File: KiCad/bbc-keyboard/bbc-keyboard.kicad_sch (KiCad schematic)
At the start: 29 parts

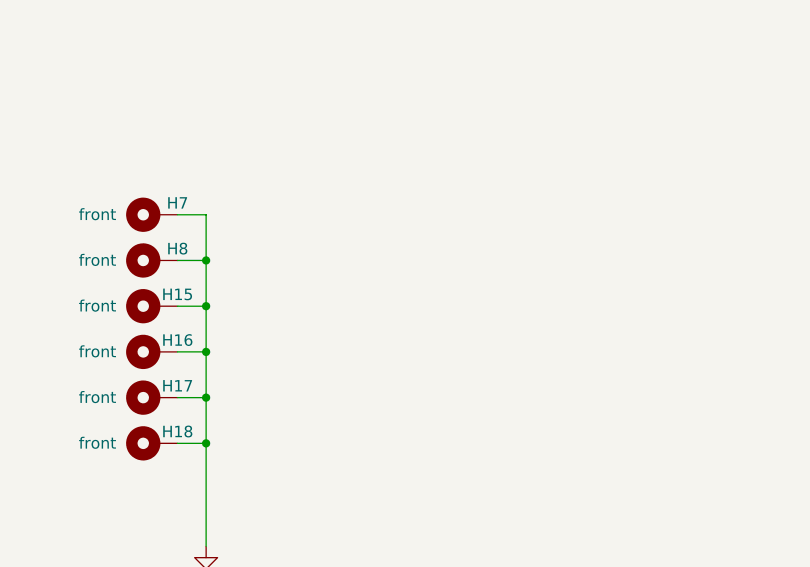
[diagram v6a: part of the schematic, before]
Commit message: mounting holes, symbols for stabilizers
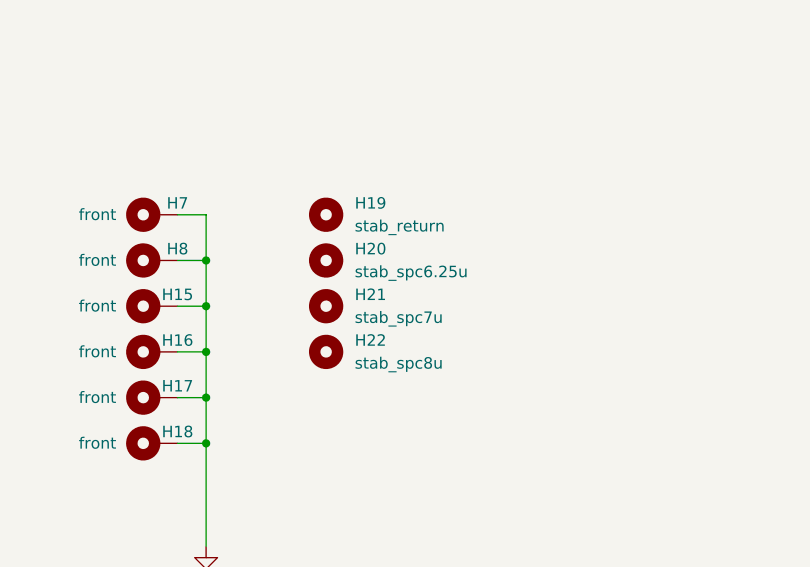
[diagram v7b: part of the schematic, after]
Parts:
- added H19: stab_return, Mounting_Keyboard_Stabilizer:Stabilizer_Cherry_MX_2.00u, symbol Mechanical:MountingHole
- added H20: stab_spc6.25u, Mounting_Keyboard_Stabilizer:Stabilizer_Cherry_MX_6.25u, symbol Mechanical:MountingHole
- added H21: stab_spc7u, Mounting_Keyboard_Stabilizer:Stabilizer_Cherry_MX_7.00u, symbol Mechanical:MountingHole
- added H22: stab_spc8u, Mounting_Keyboard_Stabilizer:Stabilizer_Cherry_MX_8.00u, symbol Mechanical:MountingHole
- H10, H11, H12, H13, H14, H9: footprint MountingHole:MountingHole_6.5mm -> Holes:SquareHole_6.5mm
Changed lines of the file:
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@@
       (effects (font (size 1.27 1.27)) (justify left))
     )
-    (property "Footprint" "MountingHole:MountingHole_6.5mm" (id 2) (at 57.15 160.655 0)
+    (property "Footprint" "Holes:SquareHole_6.5mm" (id 2) (at 57.15 160.655 0)
       (effects (font (size 1.27 1.27)) hide)
     )
@@
       (effects (font (size 1.27 1.27)) (justify left))
     )
-    (property "Footprint" "MountingHole:MountingHole_6.5mm" (id 2) (at 57.15 155.575 0)
+    (property "Footprint" "Holes:SquareHole_6.5mm" (id 2) (at 57.15 155.575 0)
       (effects (font (size 1.27 1.27)) hide)
     )
@@
       (effects (font (size 1.27 1.27)) (justify left))
     )
-    (property "Footprint" "MountingHole:MountingHole_6.5mm" (id 2) (at 57.15 150.495 0)
+    (property "Footprint" "Holes:SquareHole_6.5mm" (id 2) (at 57.15 150.495 0)
       (effects (font (size 1.27 1.27)) hide)
     )
@@
       (effects (font (size 1.27 1.27)) (justify left))
     )
-    (property "Footprint" "MountingHole:MountingHole_6.5mm" (id 2) (at 57.15 165.735 0)
+    (property "Footprint" "Holes:SquareHole_6.5mm" (id 2) (at 57.15 165.735 0)
       (effects (font (size 1.27 1.27)) hide)
     )
@@
     (pin "1")
   )
+  (symbol (lib_id "Mechanical:MountingHole") (at 109.855 150.495 0) (unit 1)
+    (in_bom yes) (on_board yes) (fields_autoplaced)
+    (property "Reference" "H21" (id 0) (at 113.03 149.2249 0)
+      (effects (font (size 1.27 1.27)) (justify left))
+    )
+    (property "Value" "stab_spc7u" (id 1) (at 113.03 151.7649 0)
+      (effects (font (size 1.27 1.27)) (justify left))
+    )
+    (property "Footprint" "Mounting_Keyboard_Stabilizer:Stabilizer_Cherry_MX_7.00u" (id 2) (at 109.855 150.495 0)
+      (effects (font (size 1.27 1.27)) hide)
+    )
+    (property "Datasheet" "~" (id 3) (at 109.855 150.495 0)
+      (effects (font (size 1.27 1.27)) hide)
+    )
+  )
   (symbol (lib_id "Mechanical:MountingHole_Pad") (at 40.005 160.655 90) (unit 1)
     (in_bom yes) (on_board yes)
@@
     (pin "2")
   )
+  (symbol (lib_id "Mechanical:MountingHole") (at 109.855 155.575 0) (unit 1)
+    (in_bom yes) (on_board yes) (fields_autoplaced)
+    (property "Reference" "H22" (id 0) (at 113.03 154.3049 0)
+      (effects (font (size 1.27 1.27)) (justify left))
+    )
+    (property "Value" "stab_spc8u" (id 1) (at 113.03 156.8449 0)
+      (effects (font (size 1.27 1.27)) (justify left))
+    )
+    (property "Footprint" "Mounting_Keyboard_Stabilizer:Stabilizer_Cherry_MX_8.00u" (id 2) (at 109.855 155.575 0)
+      (effects (font (size 1.27 1.27)) hide)
+    )
+    (property "Datasheet" "~" (id 3) (at 109.855 155.575 0)
+      (effects (font (size 1.27 1.27)) hide)
+    )
+  )
   (symbol (lib_id "Mechanical:MountingHole") (at 57.15 140.335 0) (unit 1)
     (in_bom yes) (on_board yes) (fields_autoplaced)
@@
       (effects (font (size 1.27 1.27)) (justify left))
     )
-    (property "Footprint" "MountingHole:MountingHole_6.5mm" (id 2) (at 57.15 140.335 0)
+    (property "Footprint" "Holes:SquareHole_6.5mm" (id 2) (at 57.15 140.335 0)
       (effects (font (size 1.27 1.27)) hide)
     )
     (property "Datasheet" "~" (id 3) (at 57.15 140.335 0)
+      (effects (font (size 1.27 1.27)) hide)
+    )
+  )
+  (symbol (lib_id "Mechanical:MountingHole") (at 109.855 140.335 0) (unit 1)
+    (in_bom yes) (on_board yes) (fields_autoplaced)
+    (property "Reference" "H19" (id 0) (at 113.03 139.0649 0)
+      (effects (font (size 1.27 1.27)) (justify left))
+    )
+    (property "Value" "stab_return" (id 1) (at 113.03 141.6049 0)
+      (effects (font (size 1.27 1.27)) (justify left))
+    )
+    (property "Footprint" "Mounting_Keyboard_Stabilizer:Stabilizer_Cherry_MX_2.00u" (id 2) (at 109.855 140.335 0)
+      (effects (font (size 1.27 1.27)) hide)
+    )
+    (property "Datasheet" "~" (id 3) (at 109.855 140.335 0)
       (effects (font (size 1.27 1.27)) hide)
     )
@@
     (pin "1")
     (pin "2")
+  )
+  (symbol (lib_id "Mechanical:MountingHole") (at 109.855 145.415 0) (unit 1)
+    (in_bom yes) (on_board yes) (fields_autoplaced)
+    (property "Reference" "H20" (id 0) (at 113.03 144.1449 0)
+      (effects (font (size 1.27 1.27)) (justify left))
+    )
+    (property "Value" "stab_spc6.25u" (id 1) (at 113.03 146.6849 0)
+      (effects (font (size 1.27 1.27)) (justify left))
+    )
+    (property "Footprint" "Mounting_Keyboard_Stabilizer:Stabilizer_Cherry_MX_6.25u" (id 2) (at 109.855 145.415 0)
+      (effects (font (size 1.27 1.27)) hide)
+    )
+    (property "Datasheet" "~" (id 3) (at 109.855 145.415 0)
+      (effects (font (size 1.27 1.27)) hide)
+    )
   )
   (symbol (lib_id "Connector_Generic:Conn_01x17") (at 26.67 46.99 0) (mirror y) (unit 1)
@@
       (effects (font (size 1.27 1.27)) (justify left))
     )
-    (property "Footprint" "MountingHole:MountingHole_6.5mm" (id 2) (at 57.15 145.415 0)
+    (property "Footprint" "Holes:SquareHole_6.5mm" (id 2) (at 57.15 145.415 0)
       (effects (font (size 1.27 1.27)) hide)
     )
@@
     )
     (path "/89728ebf-3bac-4567-a498-e6be30f2bdc2"
-      (reference "H9") (unit 1) (value "HoleThru") (footprint "MountingHole:MountingHole_6.5mm")
+      (reference "H9") (unit 1) (value "HoleThru") (footprint "Holes:SquareHole_6.5mm")
     )
     (path "/bccfdfe6-224a-4fb5-8717-31cd5290140d"
-      (reference "H10") (unit 1) (value "HoleThru") (footprint "MountingHole:MountingHole_6.5mm")
+      (reference "H10") (unit 1) (value "HoleThru") (footprint "Holes:SquareHole_6.5mm")
     )
     (path "/1367a1b3-e65d-4523-b7b5-11fcc761b33d"
-      (reference "H11") (unit 1) (value "HoleThru") (footprint "MountingHole:MountingHole_6.5mm")
+      (reference "H11") (unit 1) (value "HoleThru") (footprint "Holes:SquareHole_6.5mm")
     )
     (path "/0abe5a6f-9f20-4af2-8b36-acc33871de69"
-      (reference "H12") (unit 1) (value "HoleThru") (footprint "MountingHole:MountingHole_6.5mm")
+      (reference "H12") (unit 1) (value "HoleThru") (footprint "Holes:SquareHole_6.5mm")
     )
     (path "/0a150d52-b633-42d4-87bd-a9c9d470d243"
-      (reference "H13") (unit 1) (value "HoleThru") (footprint "MountingHole:MountingHole_6.5mm")
+      (reference "H13") (unit 1) (value "HoleThru") (footprint "Holes:SquareHole_6.5mm")
     )
     (path "/6d22db17-a9f9-481c-8724-512d8d176f0e"
-      (reference "H14") (unit 1) (value "HoleThru") (footprint "MountingHole:MountingHole_6.5mm")
+      (reference "H14") (unit 1) (value "HoleThru") (footprint "Holes:SquareHole_6.5mm")
     )
     (path "/4bc8c902-5c0f-41be-a7e1-d02017b95de5"
@@
       (reference "H18") (unit 1) (value "front") (footprint "MountingHole:MountingHole_2.7mm_M2.5_DIN965_Pad")
     )
+    (path "/8f761c3e-8ca1-46cf-8183-61f58698aa65"
+      (reference "H19") (unit 1) (value "stab_return") (footprint "Mounting_Keyboard_Stabilizer:Stabilizer_Cherry_MX_2.00u")
+    )
+    (path "/9c1d3cb9-ac86-41b3-92a1-07cec5bfcd44"
+      (reference "H20") (unit 1) (value "stab_spc6.25u") (footprint "Mounting_Keyboard_Stabilizer:Stabilizer_Cherry_MX_6.25u")
+    )
+    (path "/75ad1004-a5b8-4c9e-af7a-4420d71c3152"
+      (reference "H21") (unit 1) (value "stab_spc7u") (footprint "Mounting_Keyboard_Stabilizer:Stabilizer_Cherry_MX_7.00u")
+    )
+    (path "/82c365a0-2235-4f33-badc-6bd1e8c1ca11"
+      (reference "H22") (unit 1) (value "stab_spc8u") (footprint "Mounting_Keyboard_Stabilizer:Stabilizer_Cherry_MX_8.00u")
+    )
     (path "/6149d2d9-e610-4c07-b8fa-fc11a7f5479e/9ec18c21-5abd-48d2-93f1-408c3c8d1a4f"

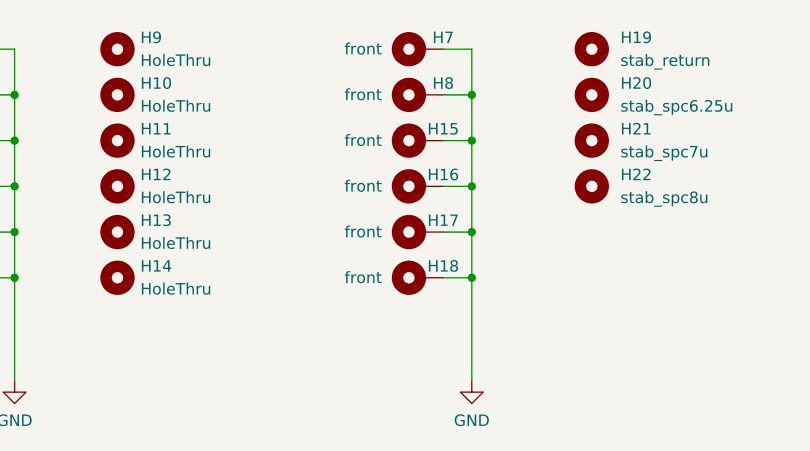
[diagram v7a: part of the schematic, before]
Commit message: Start front plate, remove H17, H18 pcb to front near space
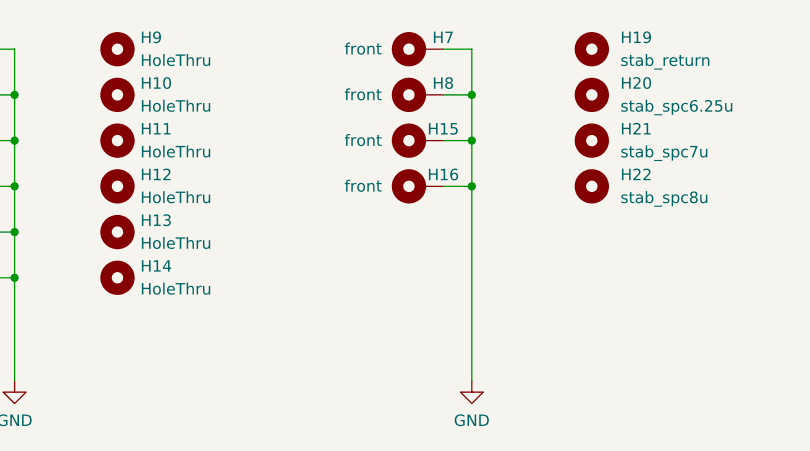
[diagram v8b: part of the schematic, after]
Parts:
- removed H17, H18: front, MountingHole:MountingHole_2.7mm_M2.5_DIN965_Pad, symbol Mechanical:MountingHole_Pad
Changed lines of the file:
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@@
   (junction (at 96.52 145.415) (diameter 0) (color 0 0 0 0)
   )
-  (junction (at 96.52 165.735) (diameter 0) (color 0 0 0 0)
-  )
   (junction (at 96.52 150.495) (diameter 0) (color 0 0 0 0)
   )
   (junction (at 237.49 113.03) (diameter 0) (color 0 0 0 0)
   )
-  (junction (at 96.52 160.655) (diameter 0) (color 0 0 0 0)
-  )
   (junction (at 45.72 155.575) (diameter 0) (color 0 0 0 0)
   )
@@
     (stroke (width 0) (type default) (color 0 0 0 0))
   )
-  (wire (pts (xy 93.345 160.655) (xy 96.52 160.655))
-    (stroke (width 0) (type default) (color 0 0 0 0))
-  )
   (wire (pts (xy 237.49 123.19) (xy 237.49 125.73))
     (stroke (width 0) (type default) (color 0 0 0 0))
@@
     (stroke (width 0) (type default) (color 0 0 0 0))
   )
-  (wire (pts (xy 96.52 160.655) (xy 96.52 165.735))
-    (stroke (width 0) (type default) (color 0 0 0 0))
-  )
   (wire (pts (xy 173.355 47.625) (xy 182.88 47.625))
     (stroke (width 0) (type default) (color 0 0 0 0))
@@
     (stroke (width 0) (type default) (color 0 0 0 0))
   )
-  (wire (pts (xy 93.345 165.735) (xy 96.52 165.735))
-    (stroke (width 0) (type default) (color 0 0 0 0))
-  )
   (wire (pts (xy 227.33 125.73) (xy 232.41 125.73))
     (stroke (width 0) (type default) (color 0 0 0 0))
@@
     (stroke (width 0) (type default) (color 0 0 0 0))
   )
-  (wire (pts (xy 96.52 165.735) (xy 96.52 177.165))
-    (stroke (width 0) (type default) (color 0 0 0 0))
-  )
   (wire (pts (xy 247.65 113.03) (xy 247.65 115.57))
     (stroke (width 0) (type default) (color 0 0 0 0))
@@
     (stroke (width 0) (type default) (color 0 0 0 0))
   )
-  (wire (pts (xy 96.52 155.575) (xy 96.52 160.655))
+  (wire (pts (xy 96.52 155.575) (xy 96.52 177.165))
     (stroke (width 0) (type default) (color 0 0 0 0))
   )
@@
     (pin "1")
     (pin "2")
-  )
-  (symbol (lib_id "Mechanical:MountingHole_Pad") (at 90.805 165.735 90) (unit 1)
-    (in_bom yes) (on_board yes)
-    (property "Reference" "H18" (id 0) (at 93.345 164.465 90))
-    (property "Value" "front" (id 1) (at 84.455 165.735 90))
-    (property "Footprint" "MountingHole:MountingHole_2.7mm_M2.5_DIN965_Pad" (id 2) (at 90.805 165.735 0)
-      (effects (font (size 1.27 1.27)) hide)
-    )
-    (property "Datasheet" "~" (id 3) (at 90.805 165.735 0)
-      (effects (font (size 1.27 1.27)) hide)
-    )
-    (pin "1")
   )
   (symbol (lib_id "Device:R") (at 59.69 67.31 90) (unit 1)
@@
     (pin "2")
   )
-  (symbol (lib_id "Mechanical:MountingHole_Pad") (at 90.805 160.655 90) (unit 1)
-    (in_bom yes) (on_board yes)
-    (property "Reference" "H17" (id 0) (at 93.345 159.385 90))
-    (property "Value" "front" (id 1) (at 84.455 160.655 90))
-    (property "Footprint" "MountingHole:MountingHole_2.7mm_M2.5_DIN965_Pad" (id 2) (at 90.805 160.655 0)
-      (effects (font (size 1.27 1.27)) hide)
-    )
-    (property "Datasheet" "~" (id 3) (at 90.805 160.655 0)
-      (effects (font (size 1.27 1.27)) hide)
-    )
-    (pin "1")
-  )
   (symbol (lib_id "Mechanical:MountingHole_Pad") (at 40.005 150.495 90) (unit 1)
     (in_bom yes) (on_board yes)
@@
       (reference "H16") (unit 1) (value "front") (footprint "MountingHole:MountingHole_2.7mm_M2.5_DIN965_Pad")
     )
-    (path "/cf52bc0a-0343-4f07-9154-308cc557e20d"
-      (reference "H17") (unit 1) (value "front") (footprint "MountingHole:MountingHole_2.7mm_M2.5_DIN965_Pad")
-    )
-    (path "/7a33042c-a20b-4bf7-ad43-19eea453b94f"
-      (reference "H18") (unit 1) (value "front") (footprint "MountingHole:MountingHole_2.7mm_M2.5_DIN965_Pad")
-    )
     (path "/8f761c3e-8ca1-46cf-8183-61f58698aa65"
